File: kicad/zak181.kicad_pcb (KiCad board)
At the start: 4 copper layers, 215.3 x 92.7 mm, 119 parts, among them IC1 Z180, J1 JTAG, J10 DE15, J2 DB25_Receptacle_MountingHoles, J3 Compact Flash, J4 Speaker, J5 Keyboard, J7 DSUB-9, J8 USB C, J9 Reset, Q2 BC547, Q3 BC547, Q4 BC547, Q5 BC547, SW1 Reset, U17 LM386, U18 NE555P, U2 Z80 PIO A, U20 XC95108PC84, U21 74HC377, U22 74HC244, U23 27C64, U24 74HC166, U25 MAX232, U26 CH340N, U27 62256, U28 AS6C4008, U29 27C128, U3 AY-3-8912, U30 74HC377, U31 GAL16V8, U32 74HC157, U33 GAL16V8, U40 AS6C4008, U8 74HC138, X1 25.175 MHz, Y2 12.288 MHz

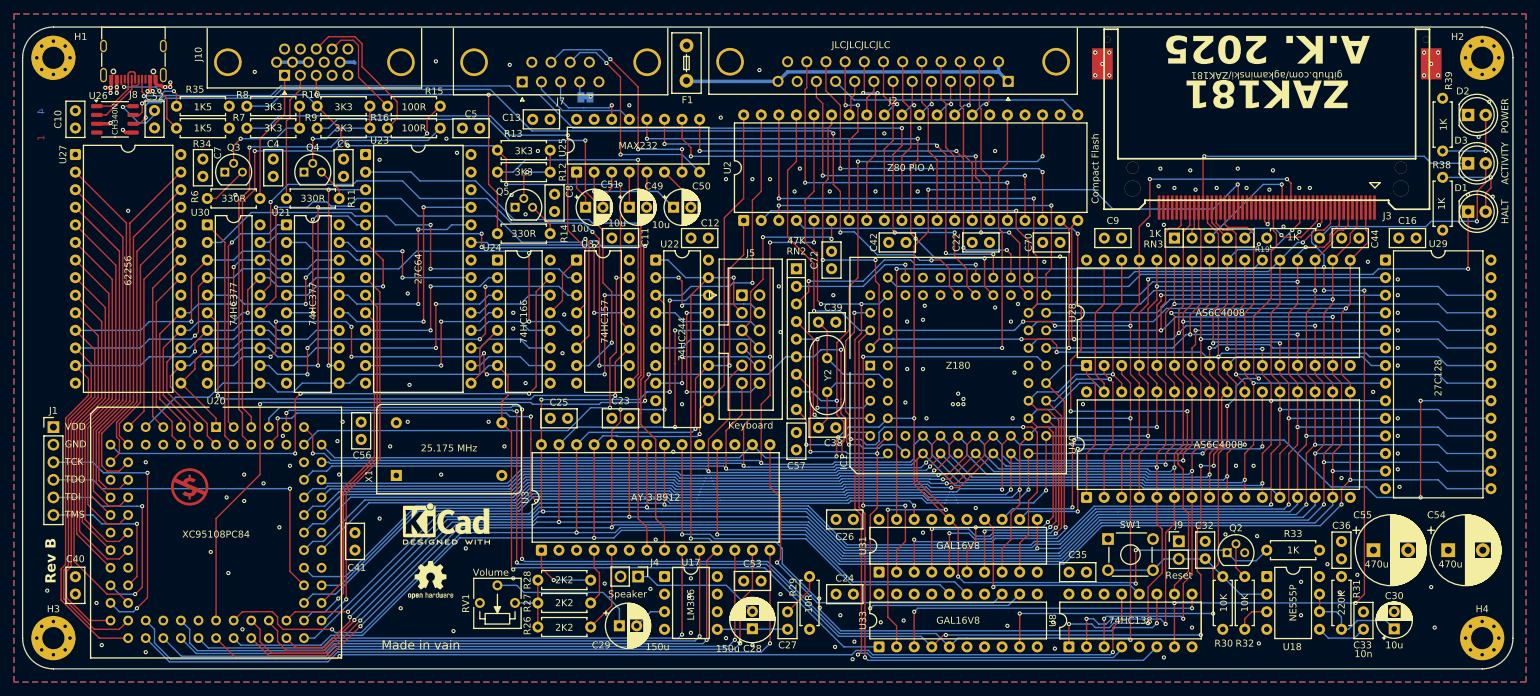
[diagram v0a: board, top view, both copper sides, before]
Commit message: hw: add RC to /RD for CF for increased compatibility
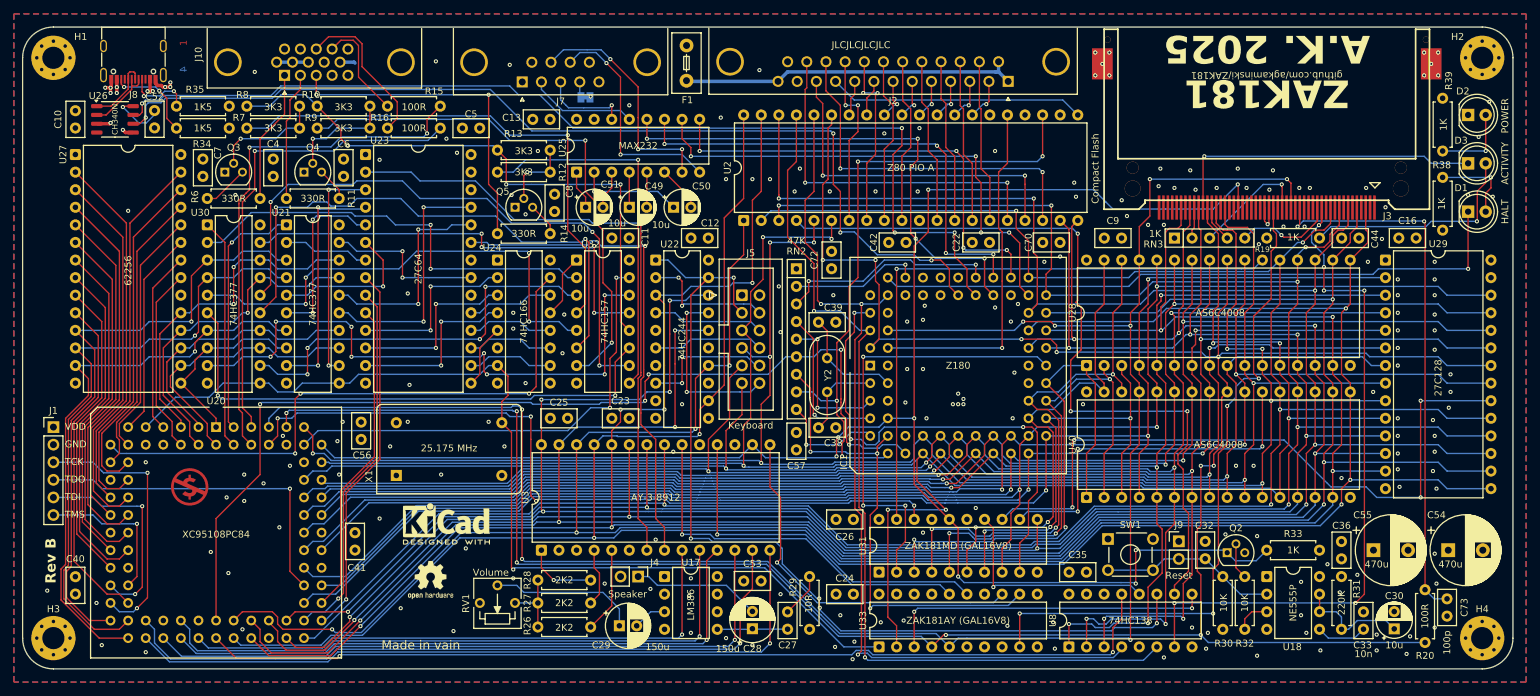
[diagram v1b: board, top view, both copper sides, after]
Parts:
- added C73: 100p, Capacitor_THT:C_Disc_D5.0mm_W2.5mm_P2.50mm, F.Cu at (232.4, 130.2)
- added R20: 100R, Resistor_THT:R_Axial_DIN0207_L6.3mm_D2.5mm_P7.62mm_Horizontal, F.Cu at (229.2, 128.9)
- U31: value GAL16V8 -> ZAK181MD (GAL16V8)
- U33: value GAL16V8 -> ZAK181AY (GAL16V8)
- moved REF** 22.7 mm to (48.6, 49.9), turned to -90 degrees
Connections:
- J3 pad 34: /cf/~{RD} -> Net-(J3-~{IORD})
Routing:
- net Net-(J3-~{IORD}): track 0.00 -> 78.5 mm, vias 0 -> 2
- net /cf/~{RD}: track 370.5 -> 388.4 mm, vias 13 -> 12
- net GND: vias 162 -> 193
